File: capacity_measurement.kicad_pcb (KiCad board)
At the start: 2 copper layers, 68.6 x 53.4 mm, 196 parts, among them J1 Ultrasound, J10 Conn_01x10, J11 Conn_01x08, J12 Conn_01x03, J13 Conn_01x03, J14 Conn_01x03, J15 Conn_01x08, J2 Conn_01x02, J3 PWR_CONN, J4 USB_B_Micro, J5 Micro_SD_Card, J6 Conn_01x08, J7 Conn_01x12, J8 Conn_01x08, J9 Conn_01x06, Q1 2N7002, Q2 2N7002, Q3 2N7002, Q4 2N7002, Q5 2N7002, SW1 SW_Push, U1 ULN2003, U10 TP4056, U11 MC34063AD, U12 HT7127-1-SOT89, U13 AMS1117-2.85, U14 ADXL343, U15 BMP280, U16 CP2102N-A01-GQFN24, U17 MPU-9250, U18 BQ25504, U2 AMS1117-5.0, U3 DS18B20, U4 ULN2003, U5 Opamp_Dual_Generic, U6 MPR121, U7 nRF52832-QFxx, U8 TagConnect, U9 SX1308, Y1 32.768k, Y2 32MHz

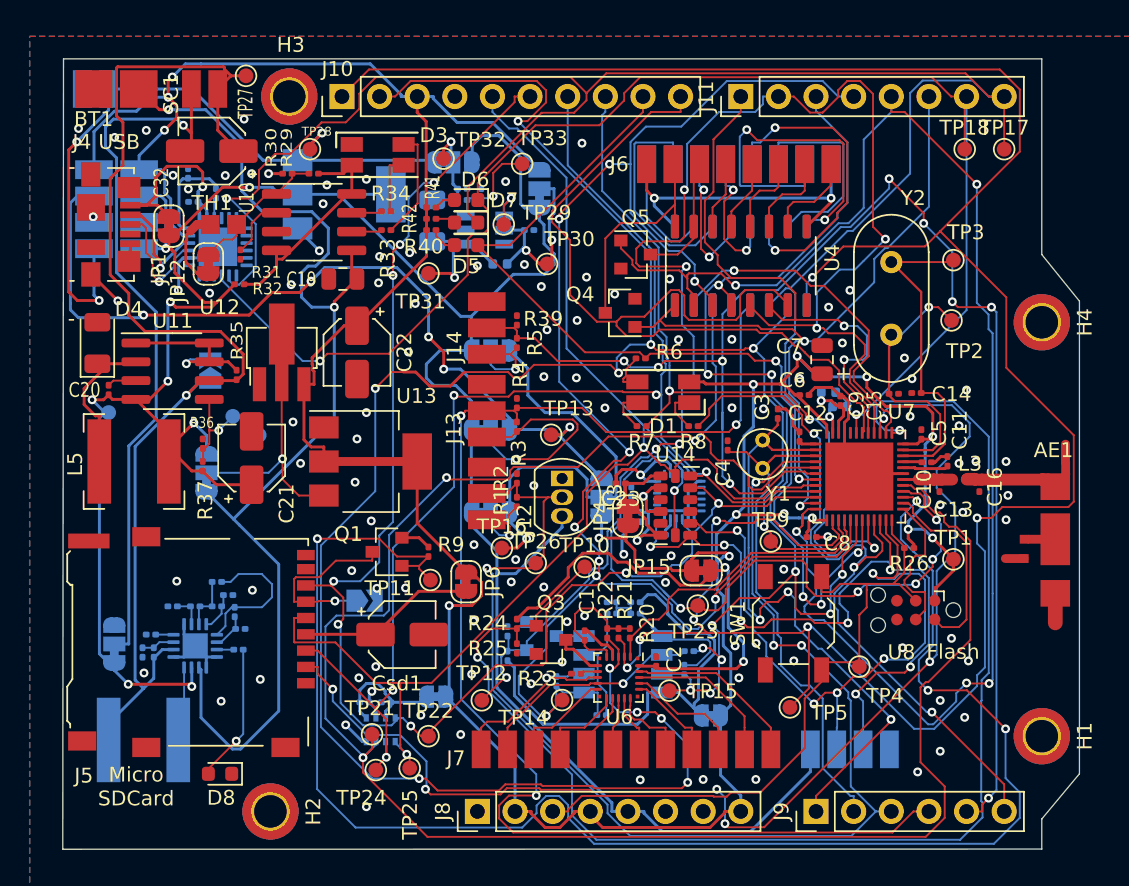
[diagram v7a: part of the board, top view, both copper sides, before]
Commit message: finished silkscreen
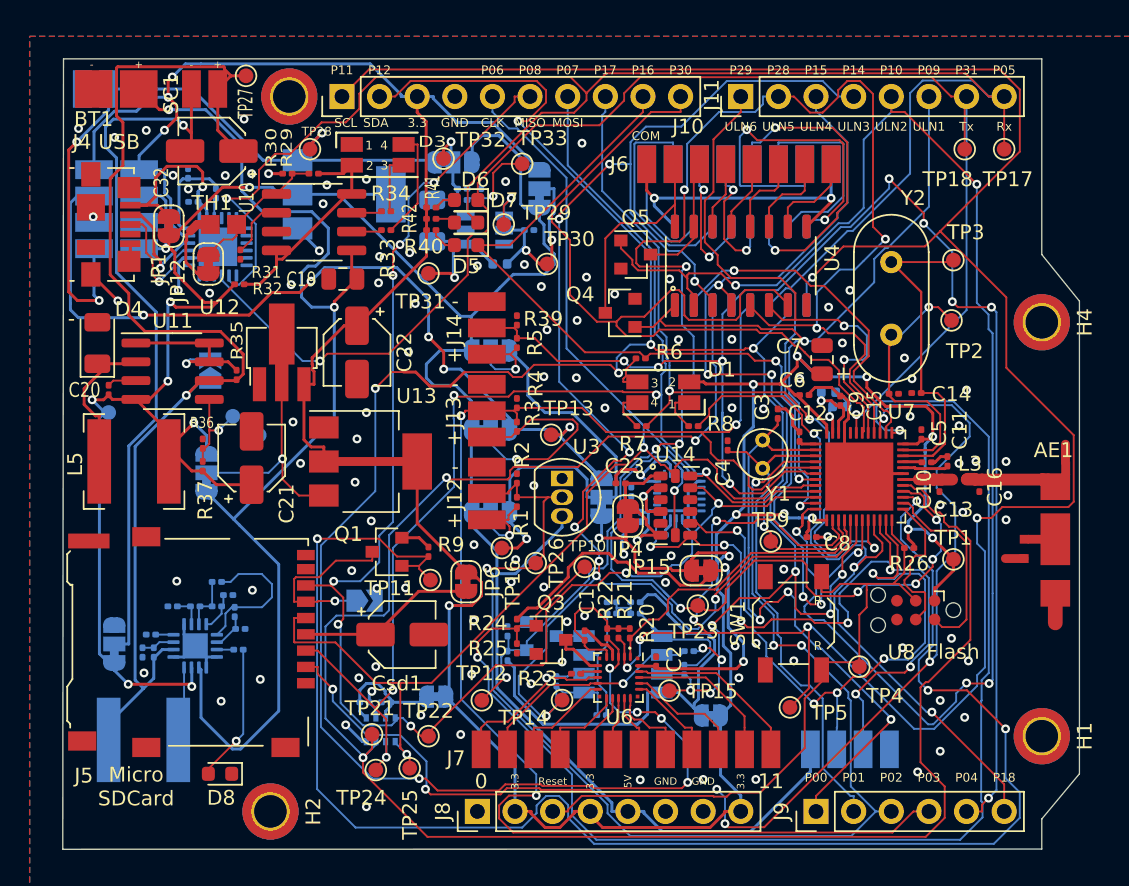
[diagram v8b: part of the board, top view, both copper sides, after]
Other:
- board text added: "0"
- board text added: "1"
- board text added: "11"
- board text added: "2"
- board text added: "3"
- board text added: "3.3"
- board text added: "4"
- board text added: "5V"
- board text added: "CLK"
- board text added: "COM"
- board text added: "GND"
- board text added: "JLCJLCJLCJLC"
- board text added: "MISO"
- board text added: "MOSI"
- board text added: "NC"
- board text added: "NRFduino tolza.xavier@gmail.com"
- board text added: "P00"
- board text added: "P01"
- board text added: "P02"
- board text added: "P03"
- board text added: "P04"
- board text added: "P05"
- board text added: "P06"
- board text added: "P07"
- board text added: "P08"
- board text added: "P09"
- board text added: "P10"
- board text added: "P11"
- board text added: "P12"
- board text added: "P14"
- board text added: "P15"
- board text added: "P16"
- board text added: "P17"
- board text added: "P18"
- board text added: "P28"
- board text added: "P29"
- board text added: "P30"
- board text added: "P31"
- board text added: "R"
- board text added: "Reset"
- board text added: "Rx"
- board text added: "SCL"
- board text added: "SDA"
- board text added: "Tx"
- board text added: "ULN1"
- board text added: "ULN2"
- board text added: "ULN3"
- board text added: "ULN4"
- board text added: "ULN5"
- board text added: "ULN6"
- board text added: "US_ECHO"
- board text added: "US_TRIG"
- board text added: "Vbat"
- board text added: "Vin"
- board text added: "VinDC"
